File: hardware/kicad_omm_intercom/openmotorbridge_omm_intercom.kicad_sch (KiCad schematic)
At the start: 0 parts

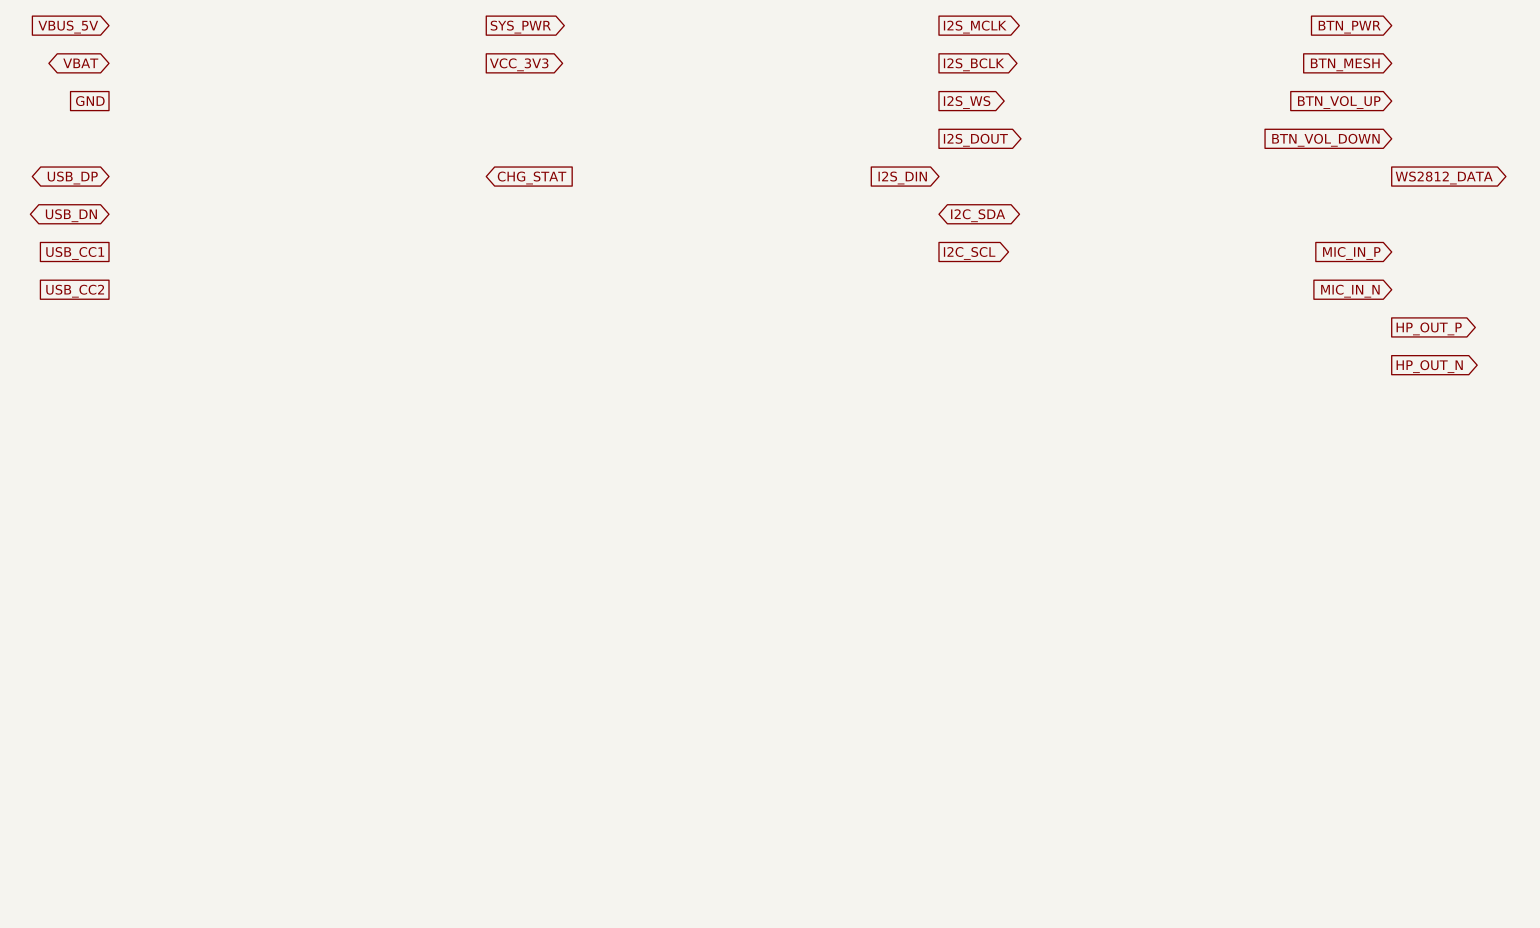
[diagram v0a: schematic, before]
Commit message: feat(system): architecture refinement v6 across hardware, firmware and docs
- Hardware:
  * PCBA 09 (OMM 2.4 GHz Intercom): Upgrade to Everest Semi ES8388 stereo codec (QFN-28)
    and Multi-Use USB-C connector (J1) combining power, WebUSB flashing and stereo audio.
  * PCBA 08 (Radar 2.0 Sub-MCU): Strict HF hardening (2x U.FL: 6.5 GHz UWB & 5.9 GHz V2X;
    no 2.4 GHz/BLE at rear), right-angle 4-pin flashing header J3.
  * PCBA 03 (Cartridge): 8-pin Kelvin-grounded audio/power header with isolated PGND/AGND.
  * CAD: Standardize DIN 934 hex nut pockets across module enclosures.

- Firmware:
  * UWB Backbone: Add multi-channel substream audio downlink (sub-channels 0/1 music,
    sub-channel 2 voice) and audio uplink packet definitions.
  * Smart Cartridge: Implement zero-latency (<1 ms) voice routing to intercom mic pin,
    A2DP music stream buffering for mesh group sharing, and 100 Hz upstream audio capture.
  * Central Box: Central DSP mixer ducking (-18 dB), voice activity detection (VAD), and
    multi-channel UWB dispatching.
  * OMM Module: Implement ES8388 stereo codec driver and I2S master duplex stream.
  * Radar Sub-MCU: Confirm 2.4 GHz RF disable and autonomous emergency strobe trigger (<1 ms).

- Documentation & WebApp:
  * Align DE & EN chapters (01, 02, 03, 04b, 07, 08, 14, 15, 16) with v6 specifications.
  * Update WebApp PWA System Builder with ES8388 stereo codec and OMM 446 PMR/DMR module.
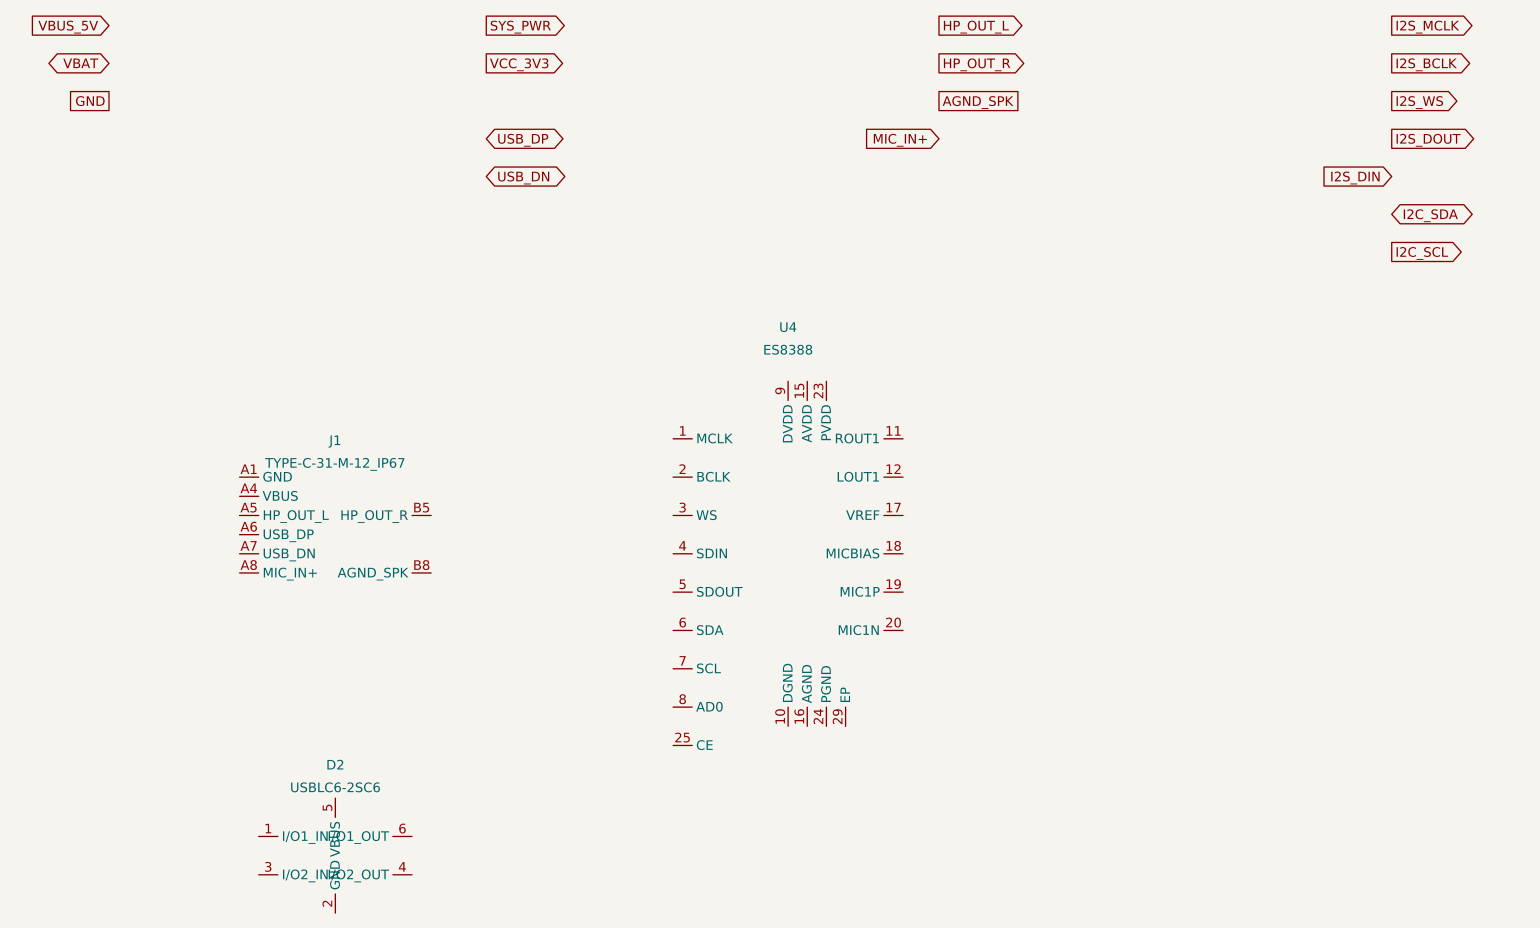
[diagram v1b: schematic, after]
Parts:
- added D2: USBLC6-2SC6, Package_TO_SOT_SMD:SOT-23-6, symbol Power:USBLC6-2SC6
- added J1: TYPE-C-31-M-12_IP67, Connector_USB:USB_C_Receptacle_HRO_TYPE-C-31-M-12, symbol Connector:USB_C_Receptacle_MultiUse
- added U4: ES8388, Package_DFN_QFN:QFN-28-1EP_4x4mm_P0.4mm_EP2.4x2.4mm, symbol Audio:ES8388
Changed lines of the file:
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@@
 (kicad_sch
-	(version 20240108)
-	(generator "openmotorbridge_gen")
+	(version 20260306)
+	(generator "eeschema")
 	(generator_version "10.0")
 	(paper "A3")
 	(title_block
 		(title "OpenMotorBridge OMM 2.4 GHz Intercom & UCS Modul (PCBA 09)")
-		(date "2026-10-02")
-		(rev "v1.1-ucs")
+		(date "2026-10-07")
+		(rev "v2.0-stereo-usb")
 		(company "OpenMotorBridge Open Source Hardware")
-		(comment 1 "ESP32-C6-MINI-1U (Direct On-Module U.FL), BQ24075 PMIC, ES8311 Codec, USB-C IP67")
+		(comment 1 "ESP32-C6-MINI-1U (U.FL), BQ24075 PMIC, ES8388 Stereo Codec, IP67 Multi-Use USB-C")
+		(comment 2 "USB-C: VBUS/GND (Power), USB_DP/DN (WebUSB Flashing via D2), HP_OUT_L/R (Stereo), MIC_IN+, AGND")
 	)
 	(global_label "VBUS_5V" (shape input) (at 30.0 30.0 180) (effects (font (size 1.27 1.27)) (justify right)))
@@
 	(global_label "VCC_3V3" (shape output) (at 80.0 35.0 0) (effects (font (size 1.27 1.27)) (justify left)))
 	(global_label "GND" (shape passive) (at 30.0 40.0 180) (effects (font (size 1.27 1.27)) (justify right)))
-	(global_label "USB_DP" (shape bidirectional) (at 30.0 50.0 180) (effects (font (size 1.27 1.27)) (justify right)))
-	(global_label "USB_DN" (shape bidirectional) (at 30.0 55.0 180) (effects (font (size 1.27 1.27)) (justify right)))
-	(global_label "USB_CC1" (shape passive) (at 30.0 60.0 180) (effects (font (size 1.27 1.27)) (justify right)))
-	(global_label "USB_CC2" (shape passive) (at 30.0 65.0 180) (effects (font (size 1.27 1.27)) (justify right)))
-	(global_label "CHG_STAT" (shape input) (at 80.0 50.0 0) (effects (font (size 1.27 1.27)) (justify left)))
-	(global_label "I2S_MCLK" (shape output) (at 140.0 30.0 0) (effects (font (size 1.27 1.27)) (justify left)))
-	(global_label "I2S_BCLK" (shape output) (at 140.0 35.0 0) (effects (font (size 1.27 1.27)) (justify left)))
-	(global_label "I2S_WS" (shape output) (at 140.0 40.0 0) (effects (font (size 1.27 1.27)) (justify left)))
-	(global_label "I2S_DOUT" (shape output) (at 140.0 45.0 0) (effects (font (size 1.27 1.27)) (justify left)))
-	(global_label "I2S_DIN" (shape input) (at 140.0 50.0 180) (effects (font (size 1.27 1.27)) (justify right)))
-	(global_label "I2C_SDA" (shape bidirectional) (at 140.0 55.0 0) (effects (font (size 1.27 1.27)) (justify left)))
-	(global_label "I2C_SCL" (shape output) (at 140.0 60.0 0) (effects (font (size 1.27 1.27)) (justify left)))
-	(global_label "BTN_PWR" (shape input) (at 200.0 30.0 180) (effects (font (size 1.27 1.27)) (justify right)))
-	(global_label "BTN_MESH" (shape input) (at 200.0 35.0 180) (effects (font (size 1.27 1.27)) (justify right)))
-	(global_label "BTN_VOL_UP" (shape input) (at 200.0 40.0 180) (effects (font (size 1.27 1.27)) (justify right)))
-	(global_label "BTN_VOL_DOWN" (shape input) (at 200.0 45.0 180) (effects (font (size 1.27 1.27)) (justify right)))
-	(global_label "WS2812_DATA" (shape output) (at 200.0 50.0 0) (effects (font (size 1.27 1.27)) (justify left)))
-	(global_label "MIC_IN_P" (shape input) (at 200.0 60.0 180) (effects (font (size 1.27 1.27)) (justify right)))
-	(global_label "MIC_IN_N" (shape input) (at 200.0 65.0 180) (effects (font (size 1.27 1.27)) (justify right)))
-	(global_label "HP_OUT_P" (shape output) (at 200.0 70.0 0) (effects (font (size 1.27 1.27)) (justify left)))
-	(global_label "HP_OUT_N" (shape output) (at 200.0 75.0 0) (effects (font (size 1.27 1.27)) (justify left)))
+	(global_label "USB_DP" (shape bidirectional) (at 80.0 45.0 0) (effects (font (size 1.27 1.27)) (justify left)))
+	(global_label "USB_DN" (shape bidirectional) (at 80.0 50.0 0) (effects (font (size 1.27 1.27)) (justify left)))
+	(global_label "HP_OUT_L" (shape output) (at 140.0 30.0 0) (effects (font (size 1.27 1.27)) (justify left)))
+	(global_label "HP_OUT_R" (shape output) (at 140.0 35.0 0) (effects (font (size 1.27 1.27)) (justify left)))
+	(global_label "AGND_SPK" (shape passive) (at 140.0 40.0 0) (effects (font (size 1.27 1.27)) (justify left)))
+	(global_label "MIC_IN+" (shape input) (at 140.0 45.0 180) (effects (font (size 1.27 1.27)) (justify right)))
+	(global_label "I2S_MCLK" (shape output) (at 200.0 30.0 0) (effects (font (size 1.27 1.27)) (justify left)))
+	(global_label "I2S_BCLK" (shape output) (at 200.0 35.0 0) (effects (font (size 1.27 1.27)) (justify left)))
+	(global_label "I2S_WS" (shape output) (at 200.0 40.0 0) (effects (font (size 1.27 1.27)) (justify left)))
+	(global_label "I2S_DOUT" (shape output) (at 200.0 45.0 0) (effects (font (size 1.27 1.27)) (justify left)))
+	(global_label "I2S_DIN" (shape input) (at 200.0 50.0 180) (effects (font (size 1.27 1.27)) (justify right)))
+	(global_label "I2C_SDA" (shape bidirectional) (at 200.0 55.0 0) (effects (font (size 1.27 1.27)) (justify left)))
+	(global_label "I2C_SCL" (shape output) (at 200.0 60.0 0) (effects (font (size 1.27 1.27)) (justify left)))
+	(symbol (lib_id "Audio:ES8388") (at 120.0 100.0 0) (unit 1)
+		(in_bom yes) (on_board yes) (dnp no)
+		(property "Reference" "U4" (at 120.0 70.0 0) (effects (font (size 1.27 1.27))))
+		(property "Value" "ES8388" (at 120.0 73.0 0) (effects (font (size 1.27 1.27))))
+		(property "Footprint" "Package_DFN_QFN:QFN-28-1EP_4x4mm_P0.4mm_EP2.4x2.4mm" (at 0 0 0) (effects (font (size 1.27 1.27)) hide))
+		(pin "1")
+		(pin "2")
+		(pin "3")
+		(pin "4")
+		(pin "5")
+		(pin "6")
+		(pin "7")
+		(pin "8")
+		(pin "9")
+		(pin "10")
+		(pin "11")
+		(pin "12")
+		(pin "15")
+		(pin "16")
+		(pin "17")
+		(pin "18")
+		(pin "19")
+		(pin "20")
+		(pin "23")
+		(pin "24")
+		(pin "25")
+		(pin "29")
+	)
+	(symbol (lib_id "Connector:USB_C_Receptacle_MultiUse") (at 60.0 100.0 0) (unit 1)
+		(in_bom yes) (on_board yes) (dnp no)
+		(property "Reference" "J1" (at 60.0 85.0 0) (effects (font (size 1.27 1.27))))
+		(property "Value" "TYPE-C-31-M-12_IP67" (at 60.0 88.0 0) (effects (font (size 1.27 1.27))))
+		(property "Footprint" "Connector_USB:USB_C_Receptacle_HRO_TYPE-C-31-M-12" (at 0 0 0) (effects (font (size 1.27 1.27)) hide))
+		(pin "A1")
+		(pin "A4")
+		(pin "A5")
+		(pin "A6")
+		(pin "A7")
+		(pin "A8")
+		(pin "B5")
+		(pin "B8")
+	)
+	(symbol (lib_id "Power:USBLC6-2SC6") (at 60.0 140.0 0) (unit 1)
+		(in_bom yes) (on_board yes) (dnp no)
+		(property "Reference" "D2" (at 60.0 128.0 0) (effects (font (size 1.27 1.27))))
+		(property "Value" "USBLC6-2SC6" (at 60.0 131.0 0) (effects (font (size 1.27 1.27))))
+		(property "Footprint" "Package_TO_SOT_SMD:SOT-23-6" (at 0 0 0) (effects (font (size 1.27 1.27)) hide))
+		(pin "1")
+		(pin "2")
+		(pin "3")
+		(pin "4")
+		(pin "5")
+		(pin "6")
+	)
 )

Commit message: feat(hw): finalize PCBA 09 OMM 2.4 GHz routing parity, schematic, 3D renders, and JLCPCB package
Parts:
- added BAT1: JST_2P_LiPo_600mAh, Connector_JST:JST_SH_BM02B-SRSS-TB_1x02-1MP_P1.00mm_Vertical, symbol Connector:Battery_JST_2Pin
- added U2: BQ24075RGTR, Package_DFN_QFN:VQFN-16-1EP_3x3mm_P0.5mm_EP1.8x1.8mm, symbol Power:BQ24075RGTR
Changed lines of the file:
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@@
 		(pin "B5")
 		(pin "B8")
+		(pin "SH")
 	)
 	(symbol (lib_id "Power:USBLC6-2SC6") (at 60.0 140.0 0) (unit 1)
@@
 		(pin "6")
 	)
+	(symbol (lib_id "Connector:Battery_JST_2Pin") (at 30.0 60.0 0) (unit 1)
+		(in_bom yes) (on_board yes) (dnp no)
+		(property "Reference" "BAT1" (at 30.0 50.0 0) (effects (font (size 1.27 1.27))))
+		(property "Value" "JST_2P_LiPo_600mAh" (at 30.0 53.0 0) (effects (font (size 1.27 1.27))))
+		(property "Footprint" "Connector_JST:JST_SH_BM02B-SRSS-TB_1x02-1MP_P1.00mm_Vertical" (at 0 0 0) (effects (font (size 1.27 1.27)) hide))
+		(pin "1")
+		(pin "2")
+		(pin "MP")
+	)
+	(symbol (lib_id "Power:BQ24075RGTR") (at 80.0 60.0 0) (unit 1)
+		(in_bom yes) (on_board yes) (dnp no)
+		(property "Reference" "U2" (at 80.0 38.0 0) (effects (font (size 1.27 1.27))))
+		(property "Value" "BQ24075RGTR" (at 80.0 41.0 0) (effects (font (size 1.27 1.27))))
+		(property "Footprint" "Package_DFN_QFN:VQFN-16-1EP_3x3mm_P0.5mm_EP1.8x1.8mm" (at 0 0 0) (effects (font (size 1.27 1.27)) hide))
+		(pin "1")
+		(pin "2")
+		(pin "3")
+		(pin "4")
+		(pin "5")
+		(pin "6")
+		(pin "7")
+		(pin "8")
+		(pin "9")
+		(pin "10")
+		(pin "11")
+		(pin "12")
+		(pin "13")
+		(pin "14")
+		(pin "15")
+		(pin "16")
+		(pin "17")
+	)
 )
